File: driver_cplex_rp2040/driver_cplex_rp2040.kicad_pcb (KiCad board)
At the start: 6 copper layers, 40.2 x 40.2 mm, 479 parts, among them J1 Conn_01x05, J2 Conn_01x05, J3 Conn_01x05, J4 Conn_01x05, J5 Conn_01x04, Q1 1xPNP and 1xNPN, Q10 1xPNP and 1xNPN, Q11 1xPNP and 1xNPN, Q12 1xPNP and 1xNPN, Q13 1xPNP and 1xNPN, Q14 1xPNP and 1xNPN, Q15 1xPNP and 1xNPN, Q16 1xPNP and 1xNPN, Q17 1xPNP and 1xNPN, Q18 1xPNP and 1xNPN, Q19 1xPNP and 1xNPN, Q2 1xPNP and 1xNPN, Q20 1xPNP and 1xNPN, Q21 1xPNP and 1xNPN, Q22 1xPNP and 1xNPN, Q23 1xPNP and 1xNPN, Q24 1xPNP and 1xNPN, Q25 1xPNP and 1xNPN, Q26 1xPNP and 1xNPN, Q27 1xPNP and 1xNPN, Q28 1xPNP and 1xNPN, Q29 1xPNP and 1xNPN, Q3 1xPNP and 1xNPN, Q30 1xPNP and 1xNPN, Q31 1xPNP and 1xNPN, Q32 1xPNP and 1xNPN, Q33 1xPNP and 1xNPN, Q34 1xPNP and 1xNPN, Q4 1xPNP and 1xNPN, Q5 1xPNP and 1xNPN, Q6 1xPNP and 1xNPN, Q7 1xPNP and 1xNPN, Q8 1xPNP and 1xNPN, Q9 1xPNP and 1xNPN, SW1 SW_Push, SW2 SW_Push, U1 AP2112K-3.3, U2 RP2040, U3 W25Q16JVUXIQ_TR, Y1 12MHz

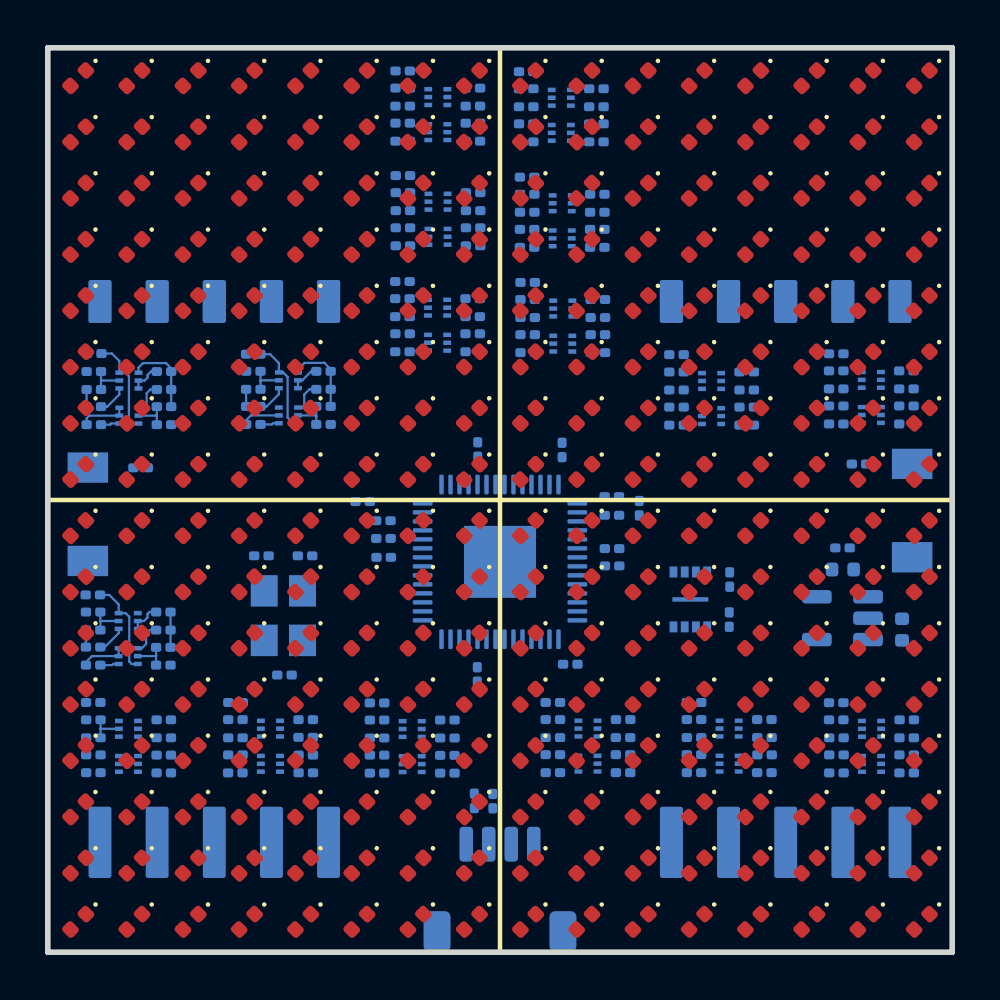
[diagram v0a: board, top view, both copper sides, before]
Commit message: Worked on layout of rp2040 cplex design.
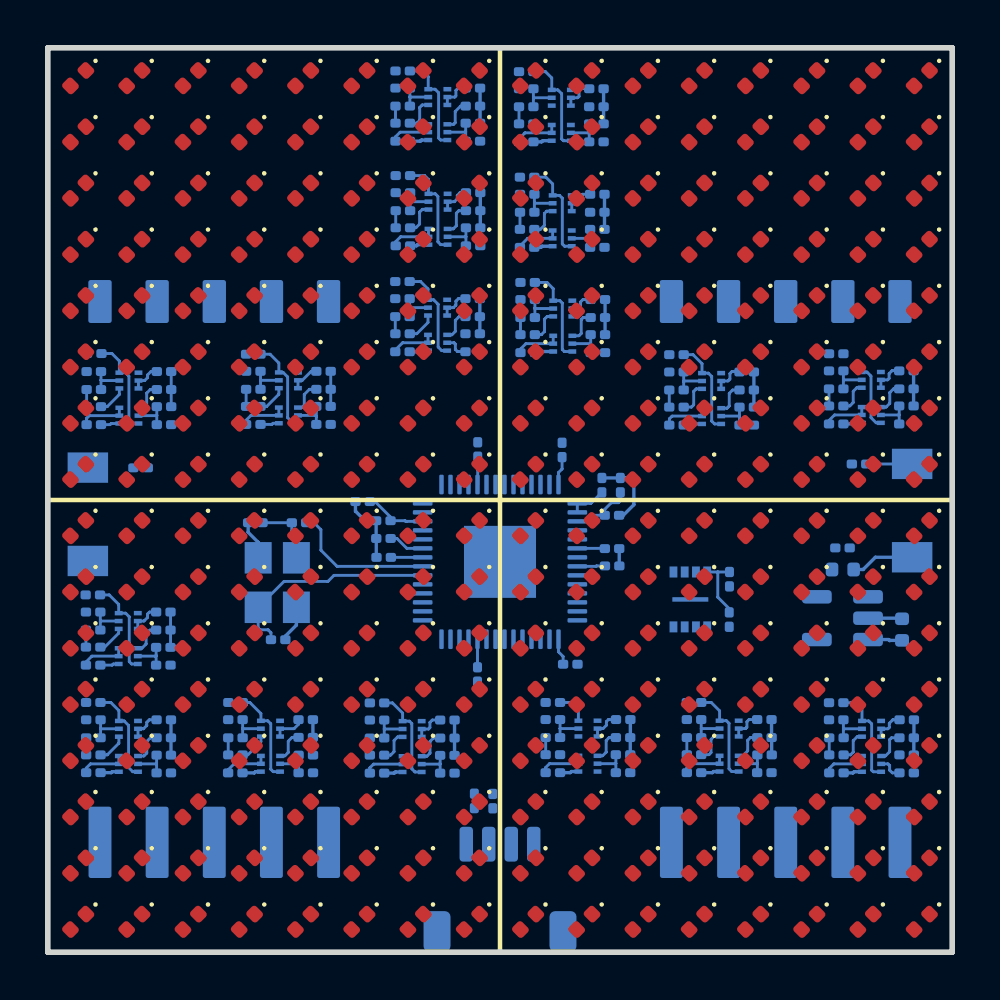
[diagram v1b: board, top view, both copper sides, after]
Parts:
- moved C4 1.59 mm to (60.1, 76.2)
- moved C5 1.49 mm to (59.1, 71.0)
- moved R3 1.49 mm to (61.1, 71.0)
- moved Y1 1.49 mm to (60.1, 73.7)
- moved C6 1.33 mm to (75.3, 69.3), turned to -90 degrees
- moved C16 0.67 mm to (74.5, 69.3), turned to -90 degrees
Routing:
- net GND: track 8.61 -> 41.6 mm
- net +3.3V: track 2.28 -> 28.0 mm
- net +5V: track 2.51 -> 15.7 mm
- net Net-(U2-XIN): track 0.00 -> 9.78 mm
- net Net-(U2-XOUT): track 0.00 -> 6.51 mm
- net +1V2: track 0.00 -> 5.66 mm
- net /level_shifter/CP_5V_07: track 0.00 -> 4.49 mm
- net /level_shifter/CP_5V_16: track 0.00 -> 4.47 mm
- net /level_shifter/CP_5V_10: track 0.00 -> 4.46 mm
- net /level_shifter/CP_5V_08: track 0.00 -> 4.45 mm
- net /level_shifter/CP_5V_11: track 0.00 -> 4.43 mm
- net /level_shifter/CP_5V_12: track 0.00 -> 4.42 mm
- net /level_shifter/CP_5V_15: track 0.00 -> 4.38 mm
- net /level_shifter/CP_5V_13: track 0.00 -> 4.35 mm
- net /level_shifter/CP_5V_06: track 0.00 -> 4.33 mm
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
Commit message: Worked on layout for rp2040 cplex'd design.
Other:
- board text added: "Pan G4 V2.0R1"
- board text removed: "Panels G4"
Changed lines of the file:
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@@
     (pad "2" smd rect (at 2.075 0 270) (size 1.35 1.8) (layers "B.Cu" "B.Paste" "B.Mask")
       (net 34 "GND") (pinfunction "2") (pintype "passive"))
+    (model "${KIPRJMOD}/panel_custom.pretty/3dmodels/tact_switch-TS-1088.step"
+      (offset (xyz 0 0 0))
+      (scale (xyz 1 1 1))
+      (rotate (xyz 0 0 90))
+    )
   )
   (footprint "panel_custom:R_0201_0603Metric" (layer "B.Cu")
@@
     (property "ki_keywords" "connector")
     (attr smd)
-    (fp_text reference "J1" (at -0.02 5.57 180 unlocked) (layer "B.SilkS")
+    (fp_text reference "J1" (at -0.02 5.57 180 unlocked) (layer "B.SilkS") hide
         (effects (font (size 1 1) (thickness 0.1)) (justify mirror))
     )
@@
     (pad "2" smd rect (at 2.075 0 90) (size 1.35 1.8) (layers "B.Cu" "B.Paste" "B.Mask")
       (net 34 "GND") (pinfunction "2") (pintype "passive"))
+    (model "${KIPRJMOD}/panel_custom.pretty/3dmodels/tact_switch-TS-1088.step"
+      (offset (xyz 0 0 0))
+      (scale (xyz 1 1 1))
+      (rotate (xyz 0 0 90))
+    )
   )
   (footprint "panel_custom:Crystal_SMD_3225-4Pin_3.2x2.5mm" (layer "B.Cu")
@@
     (property "ki_keywords" "connector")
     (attr smd)
-    (fp_text reference "J2" (at -0.02 5.57 180 unlocked) (layer "B.SilkS")
+    (fp_text reference "J2" (at -0.02 5.57 180 unlocked) (layer "B.SilkS") hide
         (effects (font (size 1 1) (thickness 0.1)) (justify mirror))
     )
@@
     (fp_line (start 7.05401 8.68299) (end -7.05401 8.68299)
       (stroke (width 0.1) (type solid)) (layer "Dwgs.User"))
-    (fp_poly
-      (pts
-        (xy 8.05101 9.67999)
-        (xy -8.05101 9.67999)
-        (xy -8.05101 -5.702)
-        (xy 8.05101 -5.702)
-        (xy 8.05101 9.67999)
-      )
-      (stroke (width 0.05) (type solid)) (fill none) (layer "B.CrtYd"))
+    (fp_rect (start -7.5 9) (end 7.5 -5)
+      (stroke (width 0.05) (type default)) (fill none) (layer "B.CrtYd"))
     (fp_line (start -6.604 -4.25399) (end -6.604 3.75)
       (stroke (width 0.1) (type solid)) (layer "B.Fab"))
@@
     (fp_line (start 7.05401 8.68299) (end -7.05401 8.68299)
       (stroke (width 0.1) (type solid)) (layer "Dwgs.User"))
-    (fp_poly
-      (pts
-        (xy 8.05101 9.67999)
-        (xy -8.05101 9.67999)
-        (xy -8.05101 -5.702)
-        (xy 8.05101 -5.702)
-        (xy 8.05101 9.67999)
-      )
-      (stroke (width 0.05) (type solid)) (fill none) (layer "B.CrtYd"))
+    (fp_rect (start -7.5 9) (end 7.5 -5)
+      (stroke (width 0.05) (type default)) (fill none) (layer "B.CrtYd"))
     (fp_line (start -6.604 -4.25399) (end -6.604 3.75)
       (stroke (width 0.1) (type solid)) (layer "B.Fab"))
@@
   (gr_line (start 51.25 63.95) (end 49.88 63.95)
     (stroke (width 0.1) (type default)) (layer "F.Fab"))
-  (gr_text "Panels G4" (at 92.4 70.1 90) (layer "B.SilkS")
+  (gr_text "Pan G4 V2.0R1" (at 70.09 65.27) (layer "B.SilkS")
     (effects (font (size 1.016 1.016) (thickness 0.2032)) (justify mirror))
   )

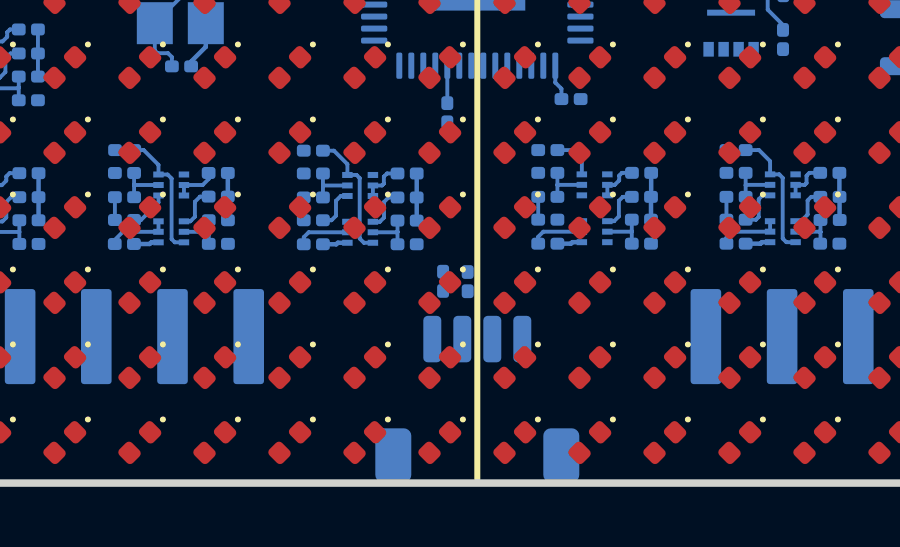
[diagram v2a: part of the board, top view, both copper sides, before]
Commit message: Added 3d model for RA 5POS conn header. Worked on layout.
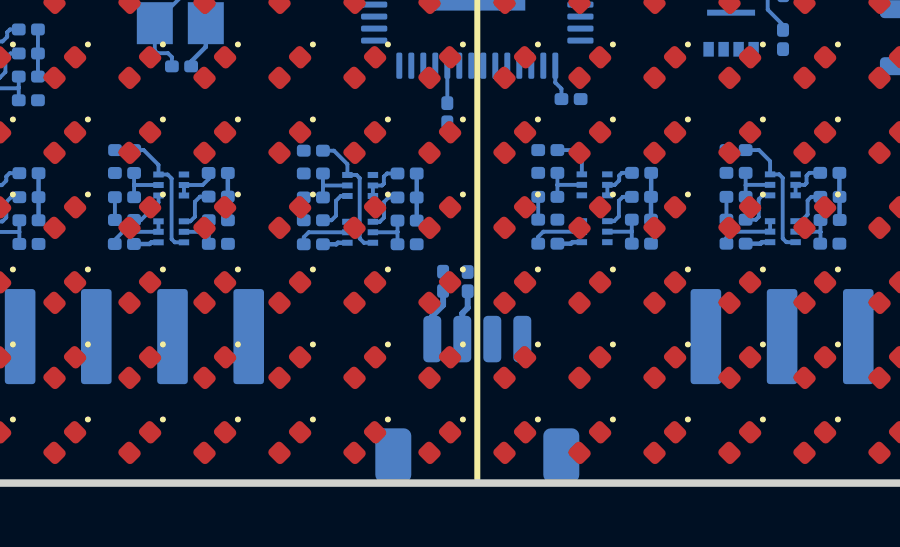
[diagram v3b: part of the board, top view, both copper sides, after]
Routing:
- net /panel_mcu/D-: track 0.00 -> 1.75 mm
- net /panel_mcu/D+: track 0.00 -> 1.67 mm
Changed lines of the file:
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@@
     (property "ki_keywords" "LED diode")
     (attr smd)
-    (fp_text reference "D80" (at 0 -0.75 -135) (layer "F.SilkS") hide
+    (fp_text reference "D80" (at 0 -0.75 45) (layer "F.SilkS") hide
         (effects (font (size 1 1) (thickness 0.15)))
     )
-    (fp_text value "LED" (at 0 1.17 -135) (layer "F.Fab") hide
+    (fp_text value "LED" (at 0 1.17 45) (layer "F.Fab") hide
         (effects (font (size 1 1) (thickness 0.15)))
     )
-    (fp_text user "${REFERENCE}" (at 0 0 -135) (layer "F.Fab")
+    (fp_text user "${REFERENCE}" (at 0 0 45) (layer "F.Fab")
         (effects (font (size 0.25 0.25) (thickness 0.04)))
     )
@@
     (pad "5" smd roundrect (at 5.08 0) (size 1.02 3.17) (layers "B.Cu" "B.Paste" "B.Mask") (roundrect_rratio 0.1)
       (net 37 "+5V") (pinfunction "Pin_5") (pintype "passive") (thermal_bridge_angle 45))
+    (model "${KIPRJMOD}/panel_custom.pretty/3dmodels/conn_header_ra_5pos.step"
+      (offset (xyz 0 4.55 1.27))
+      (scale (xyz 1 1 1))
+      (rotate (xyz 0 0 90))
+    )
   )
   (footprint "panel_custom:R_0201_0603Metric" (layer "B.Cu")
@@
     (pad "5" smd roundrect (at 5.08 0) (size 1.02 3.17) (layers "B.Cu" "B.Paste" "B.Mask") (roundrect_rratio 0.1)
       (net 58 "/panel_header/CS0") (pinfunction "Pin_5") (pintype "passive") (thermal_bridge_angle 45))
+    (model "${KIPRJMOD}/panel_custom.pretty/3dmodels/conn_header_ra_5pos.step"
+      (offset (xyz 0 4.55 1.27))
+      (scale (xyz 1 1 1))
+      (rotate (xyz 0 0 90))
+    )
   )
   (footprint "panel_custom:R_0201_0603Metric" (layer "B.Cu")
@@
   (segment (start 80.065 79.81) (end 79.76 79.81) (width 0.13) (layer "B.Cu") (net 38))
   (segment (start 80.18 81.95) (end 80.18 79.925) (width 0.13) (layer "B.Cu") (net 38))
+  (segment (start 69.68 84.26) (end 69.68 83.705) (width 0.2) (layer "B.Cu") (net 39))
+  (segment (start 69.5 85.3) (end 69.5 84.44) (width 0.2) (layer "B.Cu") (net 39))
+  (segment (start 69.5 84.44) (end 69.68 84.26) (width 0.2) (layer "B.Cu") (net 39))
+  (segment (start 68.5 84.53) (end 68.86 84.17) (width 0.2) (layer "B.Cu") (net 40))
+  (segment (start 68.5 85.3) (end 68.5 84.53) (width 0.2) (layer "B.Cu") (net 40))
+  (segment (start 68.86 84.17) (end 68.86 83.695) (width 0.2) (layer "B.Cu") (net 40))
   (segment (start 54.455 65.09) (end 54.295 65.25) (width 0.13) (layer "B.Cu") (net 41))
   (segment (start 53.93 65.9) (end 54.165 65.9) (width 0.13) (layer "B.Cu") (net 41))

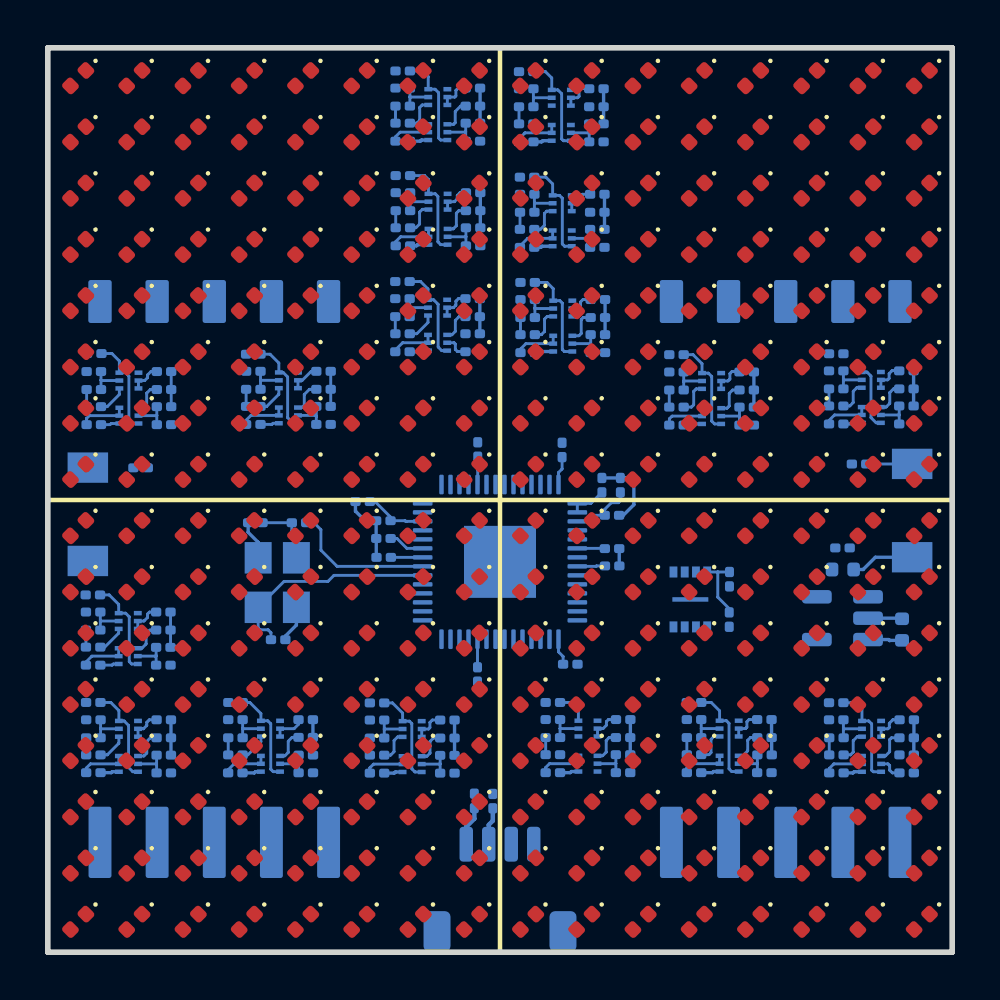
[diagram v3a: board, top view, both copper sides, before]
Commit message: Worked on layout and routing for rp2040 cplexed panel.
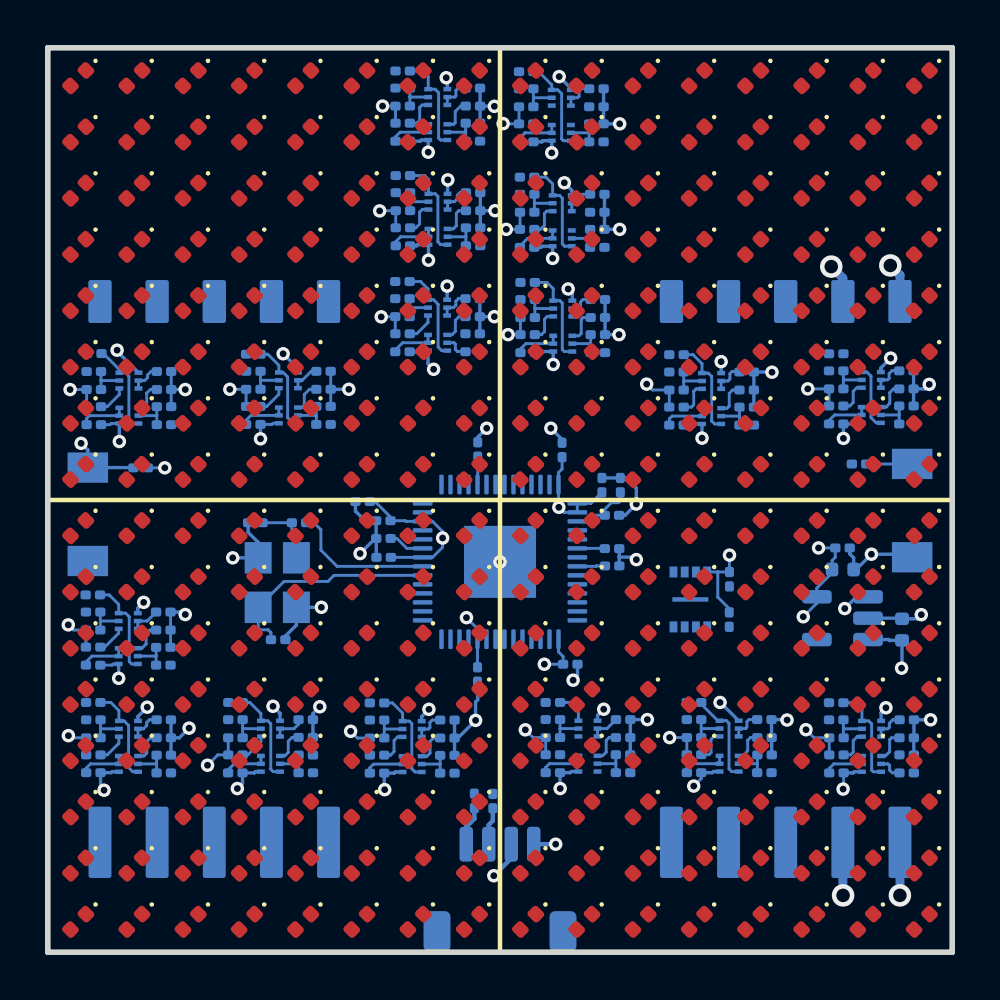
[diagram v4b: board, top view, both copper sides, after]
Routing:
- net GND: track 41.6 -> 86.2 mm, vias 0 -> 49
- net +3.3V: track 28.0 -> 55.0 mm, vias 0 -> 25
- net +5V: track 15.7 -> 36.0 mm, vias 0 -> 22
- added copper zone on In2.Cu, net +3.3V
- added copper zone on In1.Cu, net +5V
- added copper zone on In4.Cu, net GND
